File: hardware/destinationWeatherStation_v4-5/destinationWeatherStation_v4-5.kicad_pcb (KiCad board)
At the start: 2 copper layers, 63.5 x 50.8 mm, 39 parts, among them J1 S2B-PH-SM4, J2 MEM2061, J3 STEMMA_QT, Q1 IRLML6244TRPBF, Q2 IRLML6244TRPBF, Q3 DMP2035UVTQ-7, Q4 DMP2035UVTQ-7, SW1 OS102011MS2QN1, SW2 PTS647SM38SMTR2LFS, SW3 PTS647SM38SMTR2LFS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

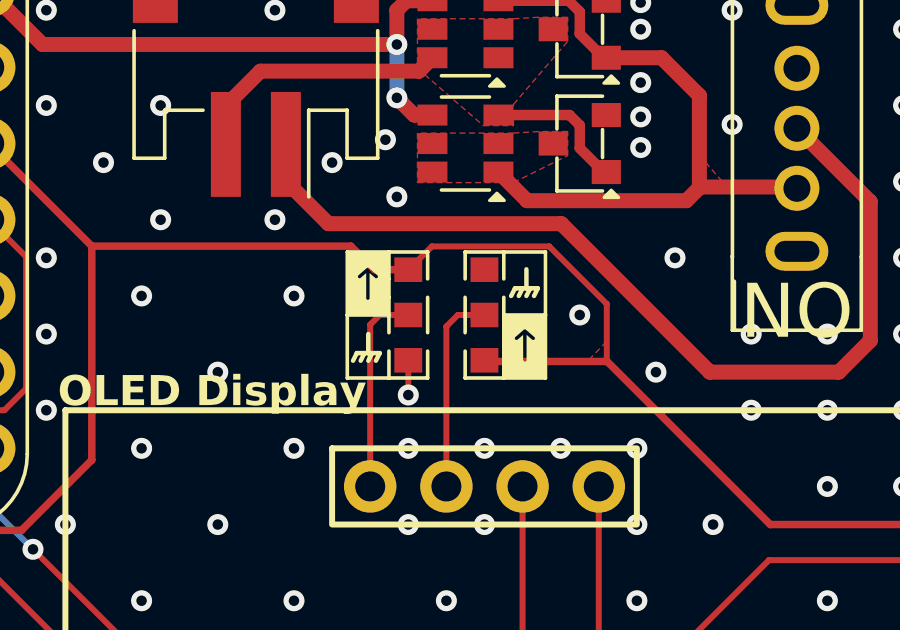
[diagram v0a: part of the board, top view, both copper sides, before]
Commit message: fixed resistor placement
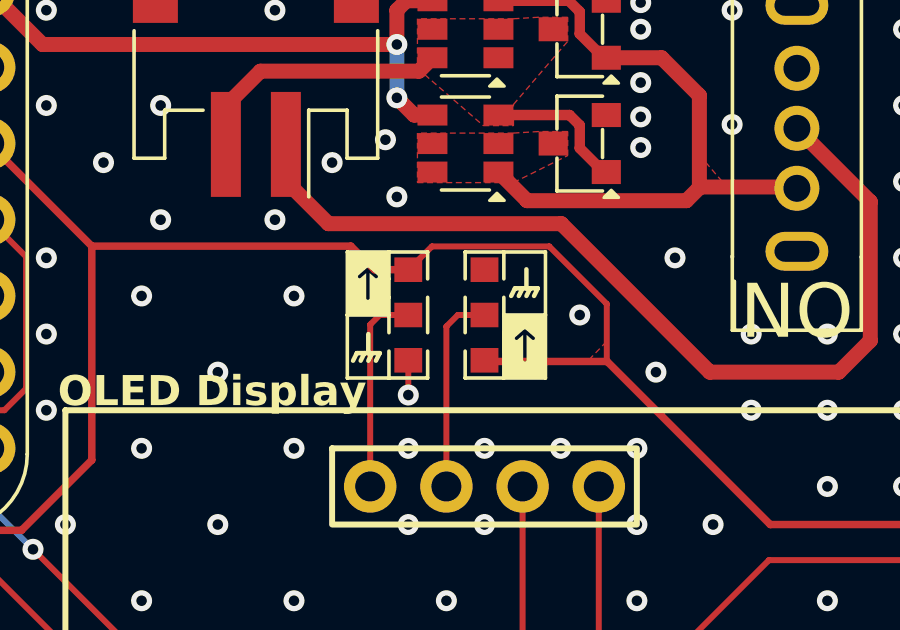
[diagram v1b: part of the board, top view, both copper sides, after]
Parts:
- moved R12 1.51 mm to (154.9, 87.8), turned to 90 degrees
- moved R11 1.51 mm to (152.4, 87.8), turned to 90 degrees
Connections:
- R11 pad 1: +3V3 -> GND
- R11 pad 3: GND -> +3V3
- R12 pad 1: GND -> +3V3
- R12 pad 3: +3V3 -> GND
